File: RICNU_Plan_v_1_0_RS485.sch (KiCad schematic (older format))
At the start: 6 parts, among them U6 SN65HVD75

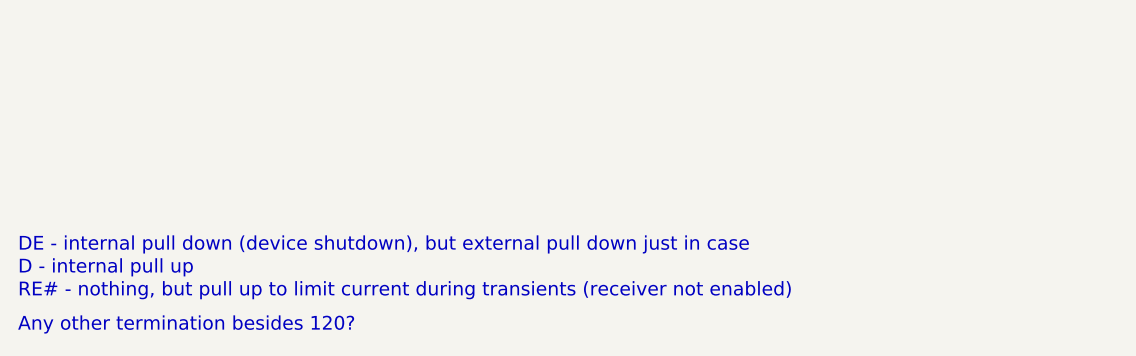
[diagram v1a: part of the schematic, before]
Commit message: Deleting PDFs
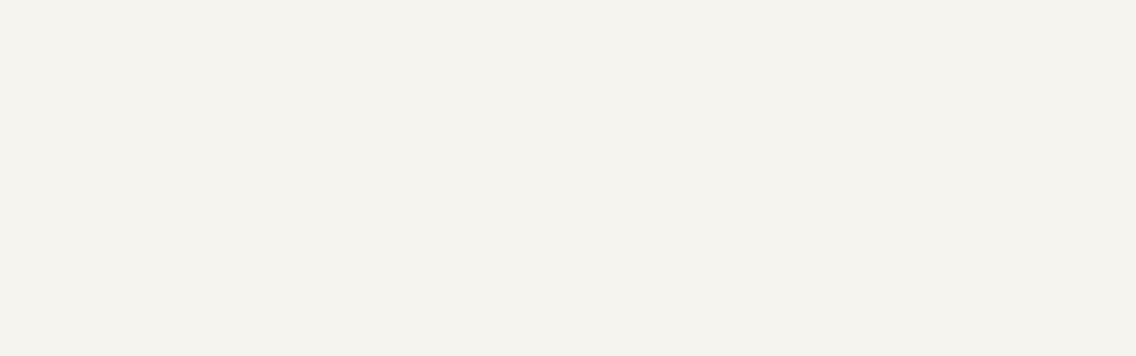
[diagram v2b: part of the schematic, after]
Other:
- note removed: "Any other termination besides 120?"
- note removed: "D - internal pull up"
- note removed: "DE - internal pull down (device shutdown), but external pull down just in case"
- note removed: "RE# - nothing, but pull up to limit current during transients (receiver not enabled)"
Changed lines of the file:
@@
 	5050 3600 5050 3800
 Connection ~ 5050 3800
-Text Notes 2500 6050 0    60   ~ 0
-DE - internal pull down (device shutdown), but external pull down just in case
-Text Notes 2500 6150 0    60   ~ 0
-D - internal pull up
-Text Notes 2500 6250 0    60   ~ 0
-RE# - nothing, but pull up to limit current during transients (receiver not enabled)
-Text Notes 2500 6400 0    60   ~ 0
-Any other termination besides 120?
 $Comp
 L R R18
